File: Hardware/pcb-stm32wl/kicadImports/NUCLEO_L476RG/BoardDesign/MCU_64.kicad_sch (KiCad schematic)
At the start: 56 parts, among them U14 MCU_LQFP64, X2 8MHz(16pF)[N/A], X3 ABS25-32.768KHZ-6-T

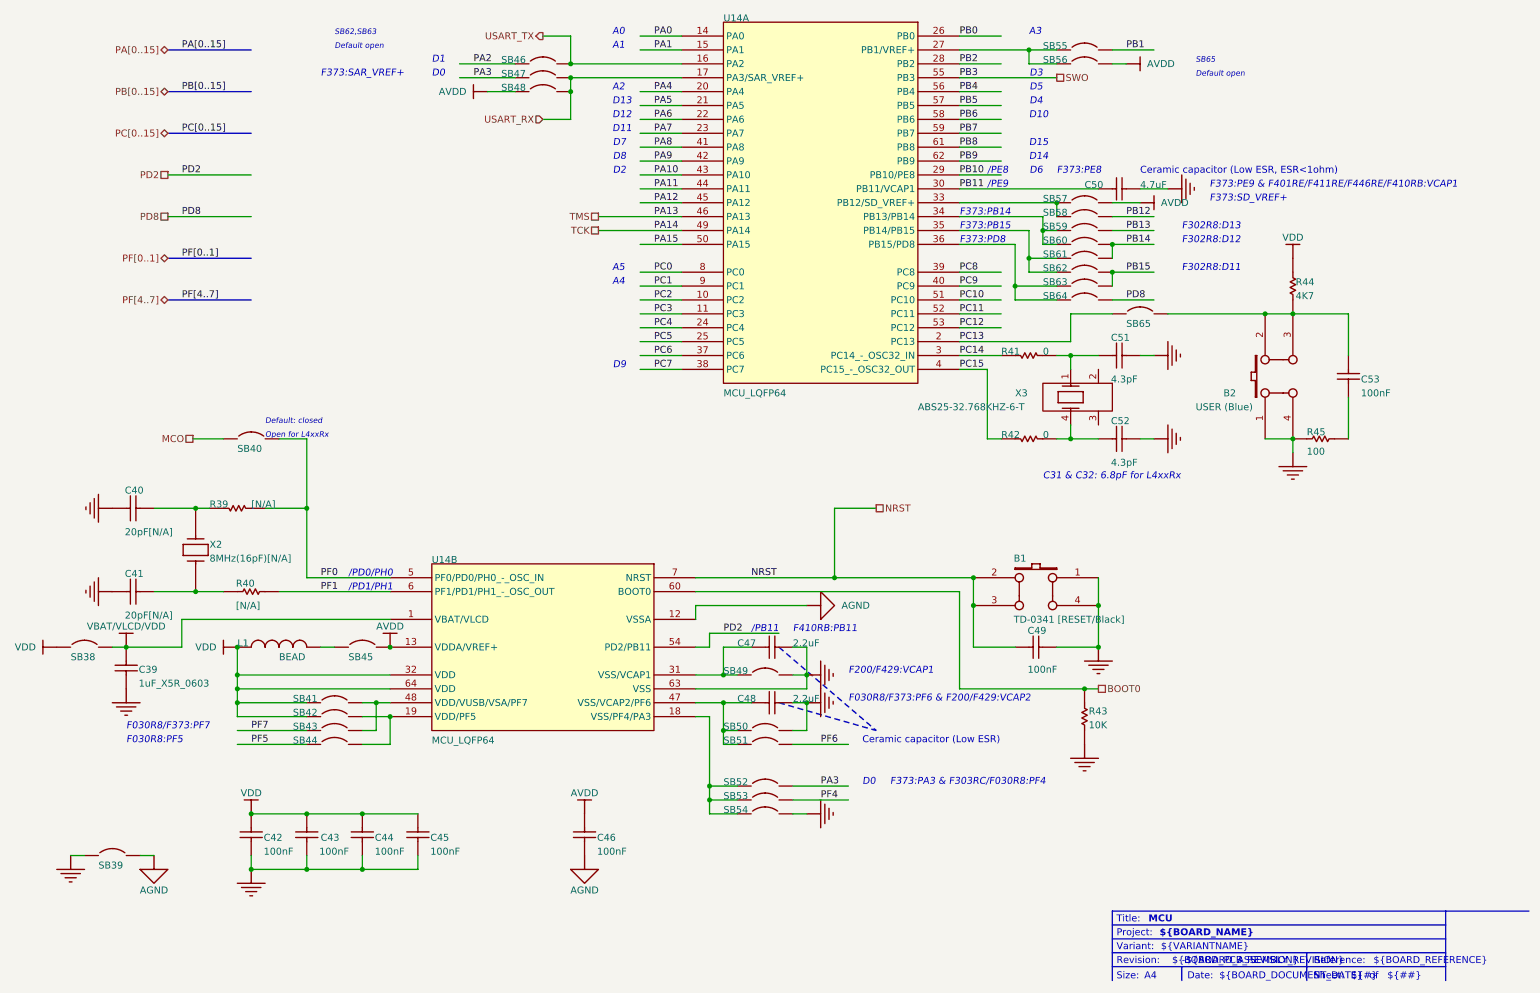
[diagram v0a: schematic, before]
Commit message: . Re-imported NUCLEO_L476RG/BoardDesign/* files using KiCad 9.0.0 one at a time (to avoid a bug evident in misconnections in MCU_64), copied the schematic contents into local kicad_sch files with the same names, prefixed with NUCLEO_L476RG_*
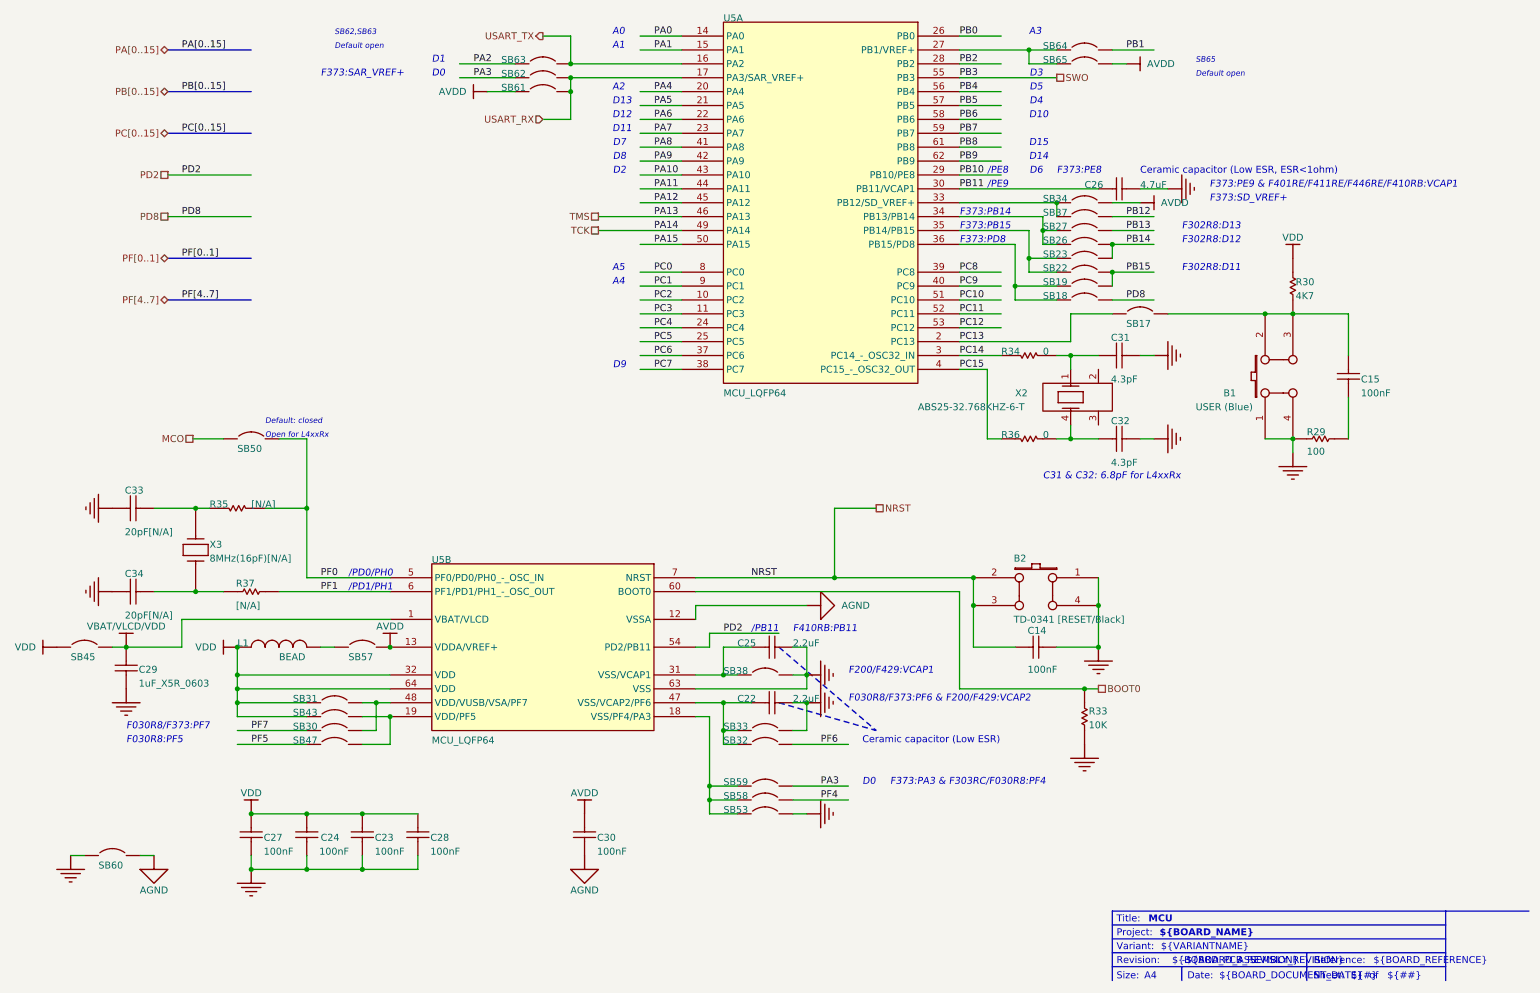
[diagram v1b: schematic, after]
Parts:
- removed B1: TD-0341 [RESET/Black], PB10, symbol Project_Overview-altium-import:U_MCU_64_0_mirrored_SW PUSHBUTTON
- removed B2: USER (Blue), PB10, symbol Project_Overview-altium-import:U_MCU_64_1_SW PUSHBUTTON
- removed C39: 1uF_X5R_0603, 0603C, symbol Project_Overview-altium-import:U_MCU_64_3_CAP SMD 0603 X5R 1µF 25V 10%
- removed C40, C41: 20pF[N/A], 0603C, symbol Project_Overview-altium-import:U_MCU_64_3_CAP_0
- removed C42, C43, C44, C45, C46: 100nF, 0603C, symbol Project_Overview-altium-import:U_MCU_64_3_Cap
- removed C47, C48: 2.2uF, TAN-A, symbol Project_Overview-altium-import:U_MCU_64_0_Cap_2.2uF_X7R_10%_0805
- removed C49: 100nF, 0603C, symbol Project_Overview-altium-import:U_MCU_64_0_mirrored_CAP
- removed C50: 4.7uF, TAN-A, symbol Project_Overview-altium-import:U_MCU_64_0_Cap_2.2uF_X7R_10%_0805
- removed C51, C52: 4.3pF, 0603C, symbol Project_Overview-altium-import:U_MCU_64_1_mirrored_CAP
- removed C53: 100nF, 0603C, symbol Project_Overview-altium-import:U_MCU_64_1_CAP
- removed L1: BEAD, 0603L, symbol Project_Overview-altium-import:U_MCU_64_0_Inductor
- removed R39: [N/A], 0603R, symbol Project_Overview-altium-import:U_MCU_64_2_mirrored_Res1_0
- removed R40: [N/A], 0603R, symbol Project_Overview-altium-import:U_MCU_64_2_Res1_0
- removed R41, R42: 0, 0603R, symbol Project_Overview-altium-import:U_MCU_64_2_mirrored_Res1_0
- removed R43: 10K, 0603R, symbol Project_Overview-altium-import:U_MCU_64_3_res1_0
- removed R44: 4K7, 0603R, symbol Project_Overview-altium-import:U_MCU_64_1_res1_0
- removed R45: 100, 0603R, symbol Project_Overview-altium-import:U_MCU_64_0_Res1_0
- removed SB38, SB39, SB40, SB41, SB42, SB43, SB44, SB45, SB46, SB47, SB48, SB49, SB50, SB51, SB52, SB53, SB54, SB55, SB56, SB57, SB58, SB59, SB60, SB61, SB62, SB63, SB64, SB65: Circuit Breaker, JP2_SMD, symbol Project_Overview-altium-import:U_MCU_64_0_Circuit Breaker
- removed U14: MCU_LQFP64, LQFP64, symbol Project_Overview-altium-import:U_MCU_64_0_MCU_LQFP64
- removed X2: 8MHz(16pF)[N/A], XTAL1, symbol Project_Overview-altium-import:U_MCU_64_1_mirrored_CRYSTAL_0
- removed X3: ABS25-32.768KHZ-6-T, XTAL_4SM_8X3R8, symbol Project_Overview-altium-import:U_MCU_64_0_MC306
- added B1: USER (Blue), PB10, symbol Top-altium-import:U_MCU_64_1_SW PUSHBUTTON_Documents.SCHLIB
- added B2: TD-0341 [RESET/Black], PB10, symbol Top-altium-import:U_MCU_64_0_mirrored_SW PUSHBUTTON_Documents.SCHLIB
- added C14: 100nF, 0603C, symbol Top-altium-import:U_MCU_64_0_mirrored_CAP_Miscellaneous Devices.IntLib
- added C15: 100nF, 0603C, symbol Top-altium-import:U_MCU_64_1_CAP_Miscellaneous Devices.IntLib
- added C22, C25: 2.2uF, TAN-A, symbol Top-altium-import:U_MCU_64_0_Cap_2.2uF_X7R_10%_0805_MCD_TOOLS.SchLib
- added C23, C24, C27, C28, C30: 100nF, 0603C, symbol Top-altium-import:U_MCU_64_3_Cap_Miscellaneous Devices.IntLib
- added C26: 4.7uF, TAN-A, symbol Top-altium-import:U_MCU_64_0_Cap_2.2uF_X7R_10%_0805_MCD_TOOLS.SchLib
- added C29: 1uF_X5R_0603, 0603C, symbol Top-altium-import:U_MCU_64_3_CAP SMD 0603 X5R 1µF 25V 10%_MB963_1.SCHLIB
- added C31, C32: 4.3pF, 0603C, symbol Top-altium-import:U_MCU_64_1_mirrored_CAP_*
- added C33, C34: 20pF[N/A], 0603C, symbol Top-altium-import:U_MCU_64_3_CAP_*_0
- added L1: BEAD, 0603L, symbol Top-altium-import:U_MCU_64_0_Inductor_Miscellaneous Devices.IntLib
- added R29: 100, 0603R, symbol Top-altium-import:U_MCU_64_0_Res1_Miscellaneous Devices.IntLib_0
- added R30: 4K7, 0603R, symbol Top-altium-import:U_MCU_64_1_res1_Miscellaneous Devices.IntLib_0
- added R33: 10K, 0603R, symbol Top-altium-import:U_MCU_64_3_res1_Miscellaneous Devices.IntLib_0
- added R34, R36: 0, 0603R, symbol Top-altium-import:U_MCU_64_2_mirrored_Res1_Miscellaneous Devices.IntLib_0
- added R35: [N/A], 0603R, symbol Top-altium-import:U_MCU_64_2_mirrored_Res1_Miscellaneous Devices.IntLib_0
- added R37: [N/A], 0603R, symbol Top-altium-import:U_MCU_64_2_Res1_Miscellaneous Devices.IntLib_0
- added SB17, SB18, SB19, SB22, SB23, SB26, SB27, SB30, SB31, SB32, SB33, SB34, SB37, SB38, SB43, SB45, SB47, SB50, SB53, SB57, SB58, SB59, SB60, SB61, SB62, SB63, SB64, SB65: Circuit Breaker, JP2_SMD, symbol Top-altium-import:U_MCU_64_0_Circuit Breaker_MCD_TOOLS.SCHLIB
- added U5: MCU_LQFP64, LQFP64, symbol Top-altium-import:U_MCU_64_0_MCU_LQFP64_MB1136.SCHLIB
- added X2: ABS25-32.768KHZ-6-T, XTAL_4SM_8X3R8, symbol Top-altium-import:U_MCU_64_0_MC306_*
- added X3: 8MHz(16pF)[N/A], XTAL1, symbol Top-altium-import:U_MCU_64_1_mirrored_CRYSTAL_*_0
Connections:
- net AGND: now also C30.2, SB60.2, U5.12 (VSSA)
- net AVDD: now also C30.1, SB34.2, SB57.2, SB61.1, SB65.2, U5.13 (VDDA/VREF+)
- net BOOT0: now also R33.1, U5.60 (BOOT0)
- net GND: now also B1.1 (A0), B1.4 (A1), B2.1 (A0), B2.4 (A1), C14.1, C22.2, C23.2, C24.2, C25.2, C26.2, C27.2, C28.2, C29.2, C31.2, C32.2, C33.2, C34.2, R29.1, R33.2, SB33.2, SB38.2, SB53.2, SB60.1, U5.63 (VSS)
- net MCO: now also SB50.1
- net NRST: now also B2.2 (B0), B2.3 (B1), C14.2, U5.7 (NRST)
- net PA0: now also U5.14 (PA0)
- net PA1: now also U5.15 (PA1)
- net PA10: now also U5.43 (PA10)
- net PA11: now also U5.44 (PA11)
- net PA12: now also U5.45 (PA12)
- net PA15: now also U5.50 (PA15)
- net PA2: now also SB63.1
- net PA3: now also SB59.2, SB62.1
- net PA4: now also U5.20 (PA4)
- net PA5: now also U5.21 (PA5)
- net PA6: now also U5.22 (PA6)
- net PA7: now also U5.23 (PA7)
- net PA8: now also U5.41 (PA8)
- net PA9: now also U5.42 (PA9)
- net PB0: now also U5.26 (PB0)
- net PB1: now also SB64.2
- net PB10: now also U5.29 (PB10/PE8)
- net PB11: now also C26.1, U5.30 (PB11/VCAP1)
- net PB12: now also SB37.2
- net PB13: now also SB27.2
- net PB14: now also SB23.2, SB26.2
- net PB15: now also SB19.2, SB22.2
- net PB2: now also U5.28 (PB2)
- net PB4: now also U5.56 (PB4)
- net PB5: now also U5.57 (PB5)
- net PB6: now also U5.58 (PB6)
- net PB7: now also U5.59 (PB7)
- net PB8: now also U5.61 (PB8)
- net PB9: now also U5.62 (PB9)
- net PC0: now also U5.8 (PC0)
- net PC1: now also U5.9 (PC1)
- net PC10: now also U5.51 (PC10)
- net PC11: now also U5.52 (PC11)
- net PC12: now also U5.53 (PC12)
- net PC13: now also SB17.1, U5.2 (PC13)
- net PC14: now also R34.2, U5.3 (PC14_-_OSC32_IN)
- net PC15: now also R36.2, U5.4 (PC15_-_OSC32_OUT)
- net PC2: now also U5.10 (PC2)
- net PC3: now also U5.11 (PC3)
- net PC4: now also U5.24 (PC4)
- net PC5: now also U5.25 (PC5)
- net PC6: now also U5.37 (PC6)
- net PC7: now also U5.38 (PC7)
- net PC8: now also U5.39 (PC8)
- net PC9: now also U5.40 (PC9)
- net PD2: now also U5.54 (PD2/PB11)
- net PD8: now also SB18.2
- net PF0: now also R35.1, SB50.2, U5.5 (PF0/PD0/PH0_-_OSC_IN)
- net PF1: now also R37.1, U5.6 (PF1/PD1/PH1_-_OSC_OUT)
- net PF4: now also SB58.2
- net PF5: now also SB47.1
- net PF6: now also SB32.2
- net PF7: now also SB30.1
- net SWO: now also U5.55 (PB3)
- net TCK: now also U5.49 (PA14)
- net TMS: now also U5.46 (PA13)
- net USART_RX: now also SB61.2, SB62.2, U5.17 (PA3/SAR_VREF+)
- net USART_TX: now also SB63.2, U5.16 (PA2)
- net VBAT/VLCD/VDD: now also C29.1, SB45.2, U5.1 (VBAT/VLCD)
- net VDD: now also C23.1, C24.1, C27.1, C28.1, L1.1, R30.2, SB31.1, SB43.1, SB45.1, U5.32 (VDD), U5.64 (VDD)
- new net: SB34.1, SB37.1, U5.33 (PB12/SD_VREF+)
- new net: B1.2 (B0), B1.3 (B1), C15.2, R30.1, SB17.2
- new net: SB64.1, SB65.1, U5.27 (PB1/VREF+)
- new net: SB26.1, SB27.1, U5.34 (PB13/PB14)
- new net: SB22.1, SB23.1, U5.35 (PB14/PB15)
- new net: SB18.1, SB19.1, U5.36 (PB15/PD8)
- new net: C22.1, SB32.1, SB33.1, U5.47 (VSS/VCAP2/PF6)
- new net: C34.1, R37.2, X3.1
- new net: SB30.2, SB31.2, U5.48 (VDD/VUSB/VSA/PF7)
- new net: C25.1, SB38.1, U5.31 (VSS/VCAP1)
- new net: C15.1, R29.2
- new net: C33.1, R35.2, X3.2
- new net: L1.2, SB57.1
- new net: C31.1, R34.1, X2.1
- new net: SB43.2, SB47.2, U5.19 (VDD/PF5)
- new net: SB53.1, SB58.1, SB59.1, U5.18 (VSS/PF4/PA3)
- new net: C32.1, R36.1, X2.4
